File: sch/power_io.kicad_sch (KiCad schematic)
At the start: 5 parts

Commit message: mp1584
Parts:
- added U?: MP1584EN-LF-Z, usb_xwitch:MP1584EN-LF-Z, symbol usb_xwitch:MP1584EN-LF-Z
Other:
- note added: "Comms / PWR from Raspberry Pi as a HAT"
- moved on the sheet: D?, J?, TP?

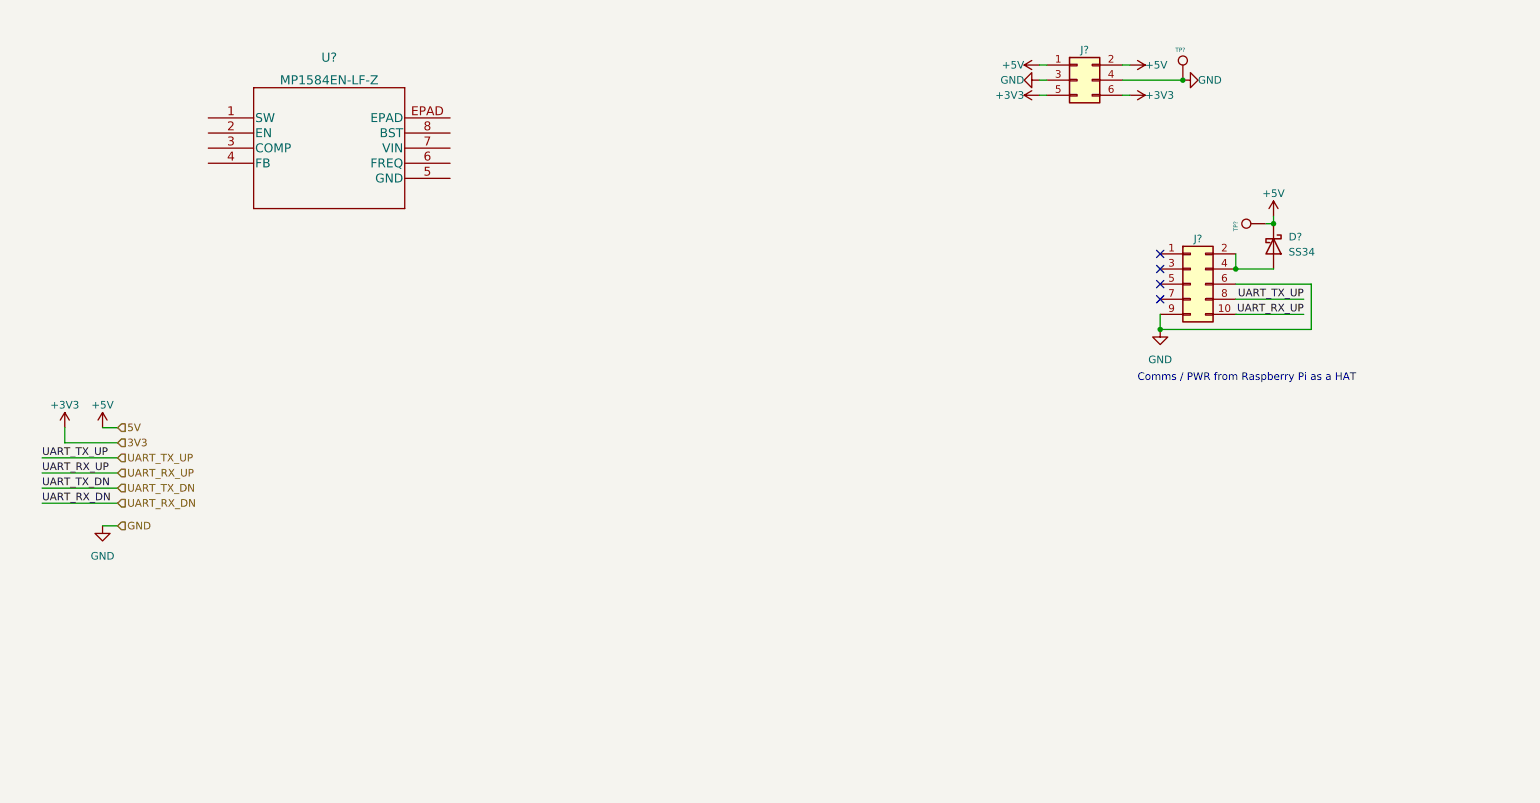
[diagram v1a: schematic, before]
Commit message: updated power circuit
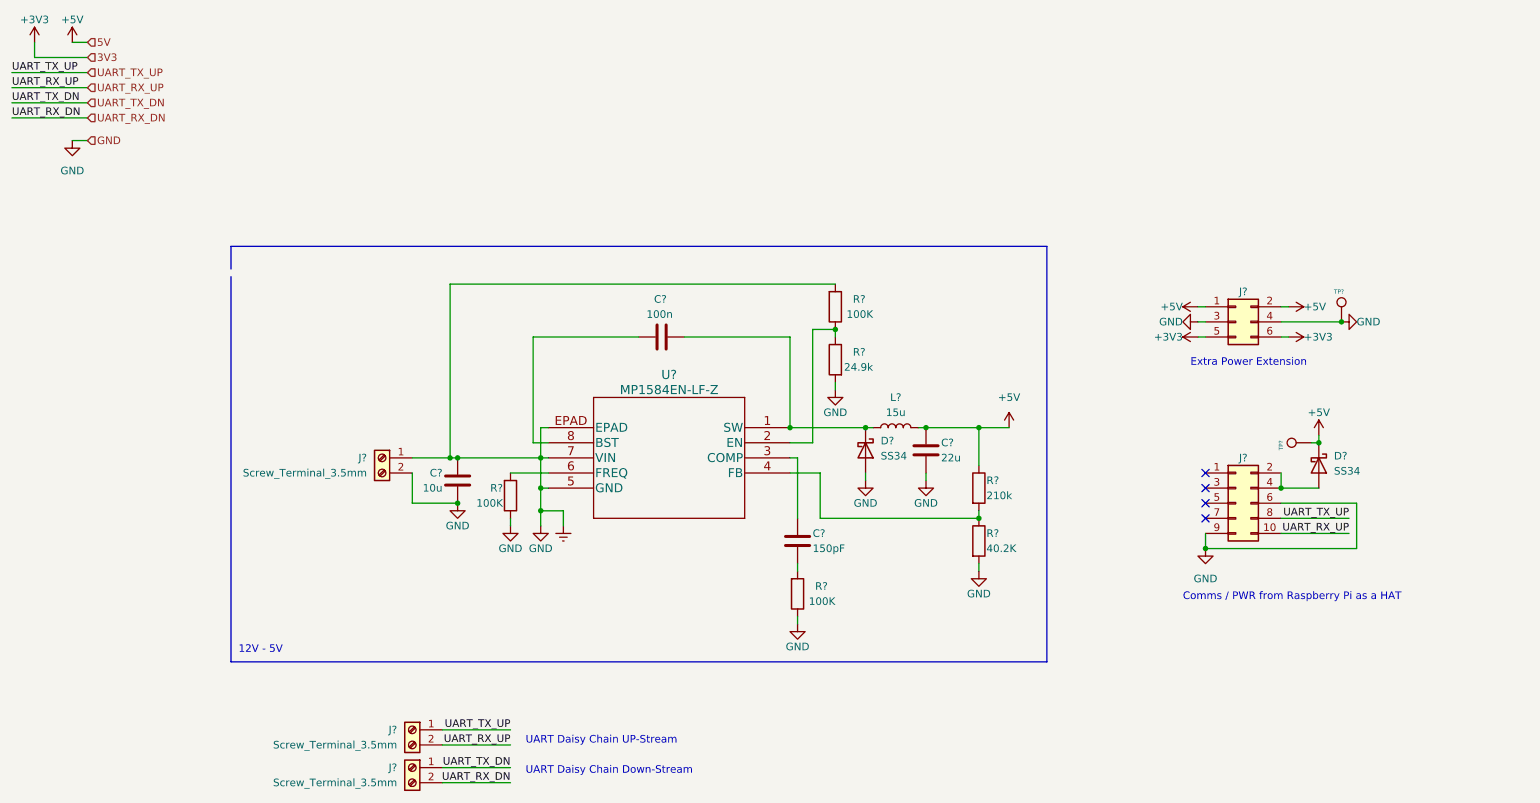
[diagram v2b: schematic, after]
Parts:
- added C?: 22u, Capacitor_SMD:C_1206_3216Metric_Pad1.33x1.80mm_HandSolder, symbol Device:C
- added C?: 100n, Resistor_SMD:R_0402_1005Metric_Pad0.72x0.64mm_HandSolder, symbol Device:C
- added C?: 10u, Capacitor_SMD:C_0805_2012Metric_Pad1.18x1.45mm_HandSolder, symbol Device:C
- added C?: 150pF, Resistor_SMD:R_0402_1005Metric_Pad0.72x0.64mm_HandSolder, symbol Device:C
- added D?: SS34, Diode_SMD:D_SMA, symbol Device:D_Schottky
- added J? (x3): Screw_Terminal_3.5mm, TerminalBlock_4Ucon:TerminalBlock_4Ucon_1x02_P3.50mm_Horizontal, symbol Connector:Screw_Terminal_01x02
- added L?: 15u, Inductor_SMD:L_12x12mm_H6mm, symbol Device:L
- added R? (x3): 100K, Resistor_SMD:R_0402_1005Metric_Pad0.72x0.64mm_HandSolder, symbol Device:R
- added R?: 210k, Resistor_SMD:R_0402_1005Metric_Pad0.72x0.64mm_HandSolder, symbol Device:R
- added R?: 24.9k, Resistor_SMD:R_0603_1608Metric_Pad0.98x0.95mm_HandSolder, symbol Device:R
- added R?: 40.2K, Resistor_SMD:R_0402_1005Metric_Pad0.72x0.64mm_HandSolder, symbol Device:R
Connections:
- net GND is gone; now on net Earth: J?.3 (Pin_3), J?.4 (Pin_4), J?.6 (Pin_6), J?.9 (Pin_9), TP?.1
- net +5V: now also C?.1, L?.2, R?.1
- net UART_RX_DN: now also J?.2 (Pin_2)
- net UART_RX_UP: now also J?.2 (Pin_2)
- net UART_TX_DN: now also J?.1 (Pin_1)
- net UART_TX_UP: now also J?.1 (Pin_1)
- net at U?.1 (SW): now also C?.1, D?.1 (K), L?.1
- net at U?.2 (EN): now also R?.1, R?.1
- net at U?.3 (COMP): now also C?.1
- net at U?.4 (FB): now also R?.1, R?.2
- net Earth: now reaches U?.5 (GND)
- net Earth: now also U?.7 (VIN), U?.EPAD, C?.1, C?.2, C?.2, D?.2 (A), J?.1 (Pin_1), J?.2 (Pin_2), R?.1, R?.1, R?.2, R?.2, R?.2
- net at U?.6 (FREQ): now also R?.2
- net at U?.8 (BST): now also C?.2
- new net: C?.2, R?.2
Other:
- note added: "12V - 5V"
- note added: "Extra Power Extension"
- note added: "UART Daisy Chain Down-Stream"
- note added: "UART Daisy Chain UP-Stream"
- moved on the sheet: D?, J?, TP?, U?

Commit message: annotated components
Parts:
- J11: renamed from J?; LCSC (none) -> C65114
- U8: renamed from U?; LCSC (none) -> C15051
- gave numbers to parts that had none: 19

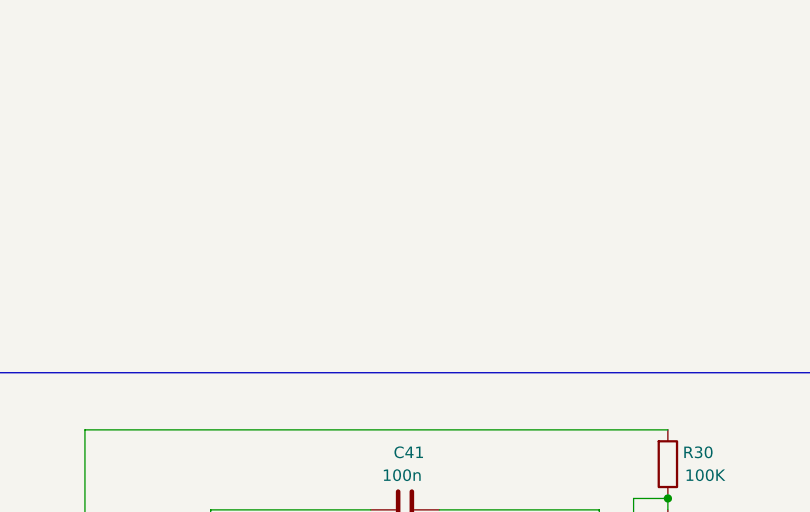
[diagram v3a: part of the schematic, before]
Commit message: drc checks and renaming
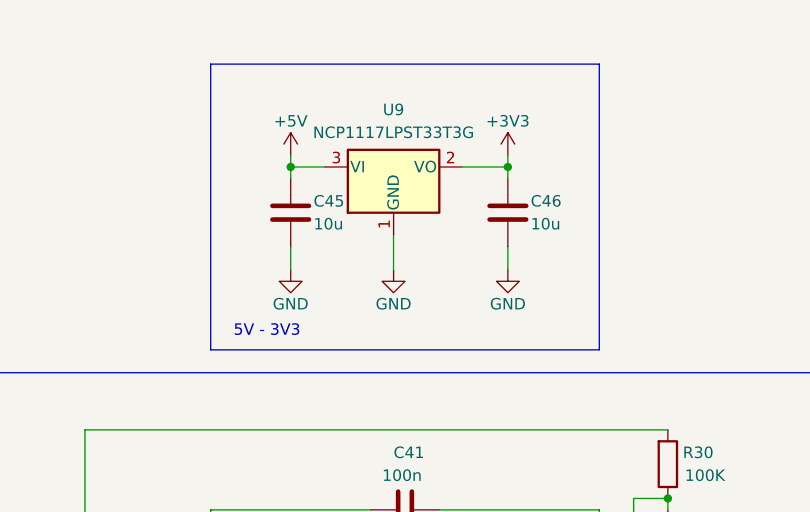
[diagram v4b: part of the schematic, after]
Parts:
- added C45, C46: 10u, Capacitor_SMD:C_0603_1608Metric_Pad1.08x0.95mm_HandSolder, symbol Device:C
- added U9: NCP1117LPST33T3G, Package_TO_SOT_SMD:SOT-223-3_TabPin2, symbol Regulator_Linear:NCP1117-3.3_SOT223
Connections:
- net +3V3: now also C46.1, U9.2 (VO)
- net +5V: now also C45.1, U9.3 (VI)
- net Earth: now also C45.2, C46.2, U9.1 (GND)
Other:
- note added: "5V - 3V3"

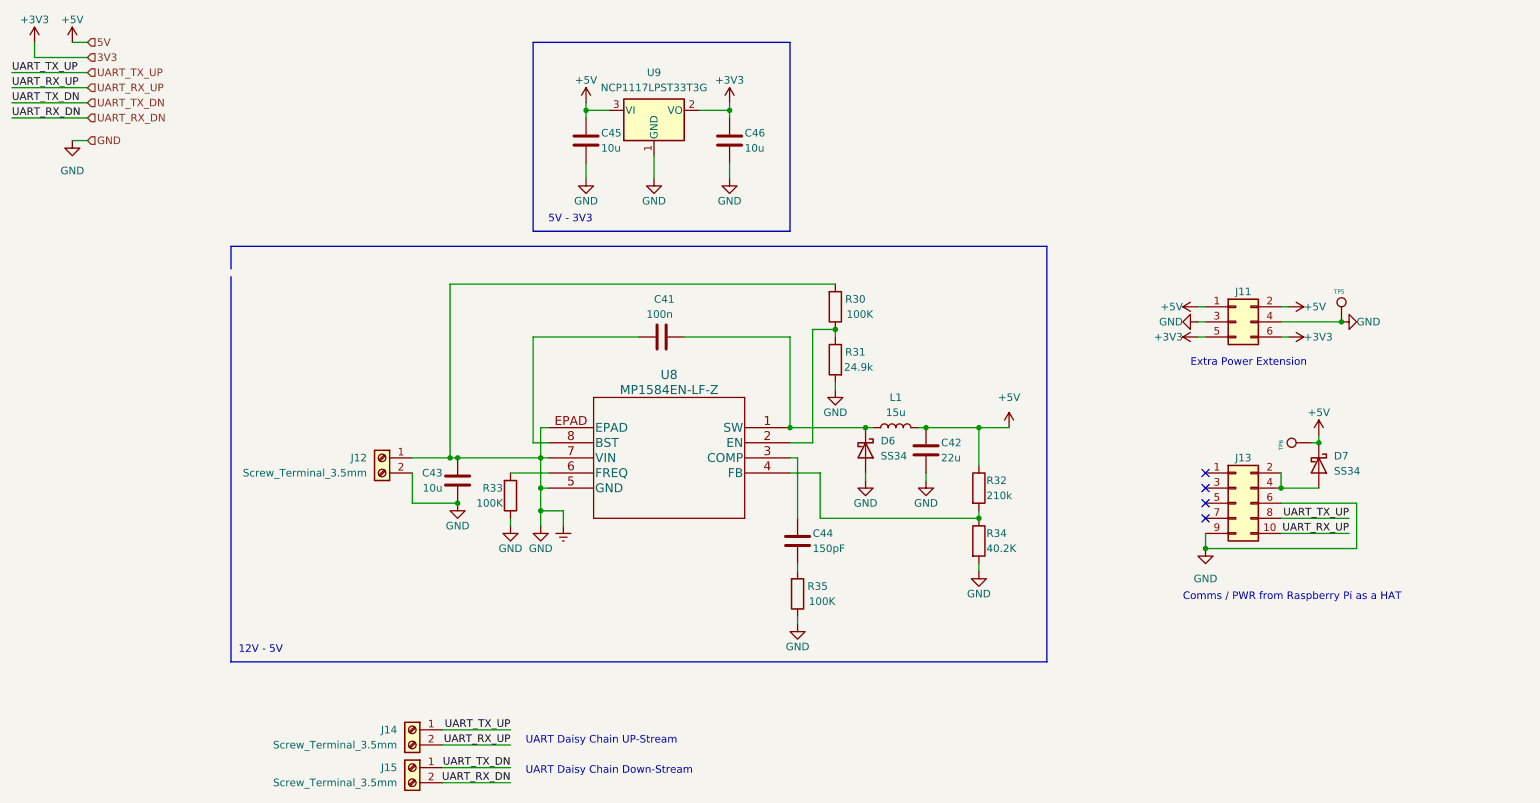
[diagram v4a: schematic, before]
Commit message: updated power on leds, hub 4 LEDs and misc
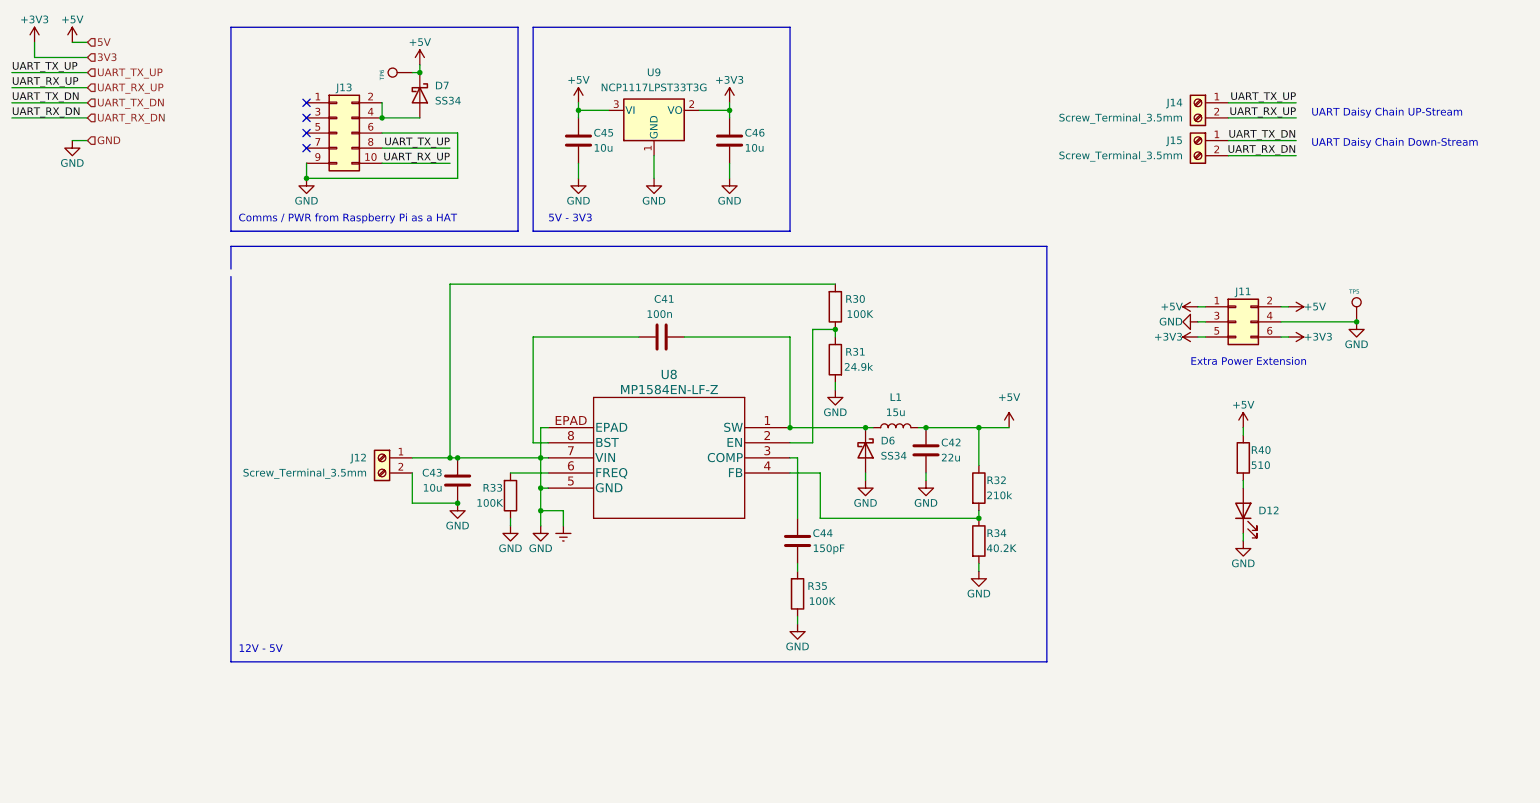
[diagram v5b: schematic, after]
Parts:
- added D12: 19-217/GHC-YR1S2/3T, Diode_SMD:D_0603_1608Metric_Pad1.05x0.95mm_HandSolder, symbol Device:LED
- added R40: 510, Resistor_SMD:R_0402_1005Metric_Pad0.72x0.64mm_HandSolder, symbol Device:R
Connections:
- net +5V: now also R40.1
- net Earth: now also D12.1 (K)
- new net: D12.2 (A), R40.2
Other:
- moved on the sheet: C45, D7, J13, J14, J15, TP5, TP6

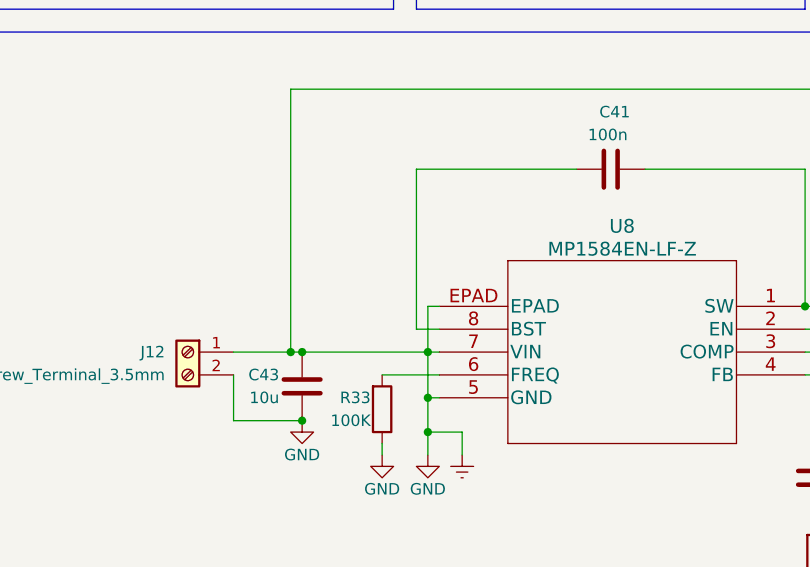
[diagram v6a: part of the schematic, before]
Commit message: fix sch unexpect to gnd; usb to right angle; pcb boarder increased to pi size
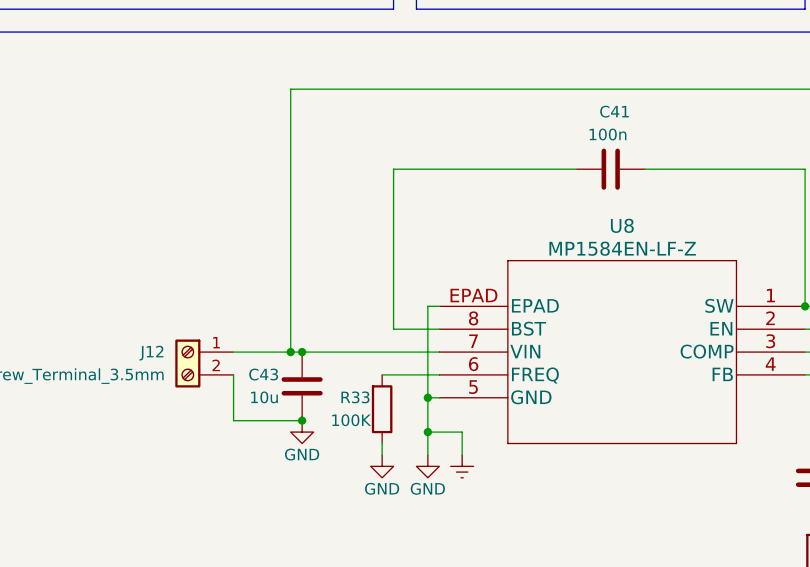
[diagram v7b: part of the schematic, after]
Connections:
- net Earth: no longer C43.1, J12.1 (Pin_1), R30.2, U8.7 (VIN)
- new net: C43.1, J12.1 (Pin_1), R30.2, U8.7 (VIN)
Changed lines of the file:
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@@
   (junction (at 124.46 41.91) (diameter 0) (color 0 0 0 0)
   )
-  (junction (at 118.11 100.33) (diameter 0) (color 0 0 0 0)
+  (junction (at 102.87 100.33) (diameter 0) (color 0 0 0 0)
   )
   (junction (at 191.77 110.49) (diameter 0) (color 0 0 0 0)
@@
   (junction (at 255.27 77.47) (diameter 0) (color 0 0 0 0)
   )
-  (junction (at 102.87 100.33) (diameter 0) (color 0 0 0 0)
-  )
   (junction (at 78.74 53.34) (diameter 0) (color 0 0 0 0)
   )
@@
   (junction (at 91.44 43.18) (diameter 0) (color 0 0 0 0)
   )
+  (junction (at 118.11 105.41) (diameter 0) (color 0 0 0 0)
+  )
   (junction (at 118.11 109.22) (diameter 0) (color 0 0 0 0)
   )
   (junction (at 97.79 35.56) (diameter 0) (color 0 0 0 0)
-  )
-  (junction (at 118.11 105.41) (diameter 0) (color 0 0 0 0)
   )
   (junction (at 104.14 100.33) (diameter 0) (color 0 0 0 0)
@@
     (stroke (width 0) (type default) (color 0 0 0 0))
   )
-  (wire (pts (xy 102.87 100.33) (xy 96.52 100.33))
-    (stroke (width 0) (type default) (color 0 0 0 0))
-  )
   (polyline (pts (xy 203.2 64.77) (xy 66.04 64.77))
     (stroke (width 0) (type default) (color 0 0 0 0))
@@
     (stroke (width 0) (type default) (color 0 0 0 0))
   )
+  (wire (pts (xy 118.11 95.25) (xy 118.11 105.41))
+    (stroke (width 0) (type default) (color 0 0 0 0))
+  )
   (wire (pts (xy 167.64 78.74) (xy 167.64 80.01))
     (stroke (width 0) (type default) (color 0 0 0 0))
@@
     (stroke (width 0) (type default) (color 0 0 0 0))
   )
-  (wire (pts (xy 118.11 100.33) (xy 118.11 105.41))
-    (stroke (width 0) (type default) (color 0 0 0 0))
-  )
   (polyline (pts (xy 66.04 134.62) (xy 203.2 134.62))
     (stroke (width 0) (type default) (color 0 0 0 0))
@@
     (stroke (width 0) (type default) (color 0 0 0 0))
   )
-  (wire (pts (xy 116.84 97.79) (xy 119.38 97.79))
-    (stroke (width 0) (type default) (color 0 0 0 0))
-  )
-  (wire (pts (xy 118.11 100.33) (xy 104.14 100.33))
+  (wire (pts (xy 114.3 97.79) (xy 119.38 97.79))
     (stroke (width 0) (type default) (color 0 0 0 0))
   )
@@
     (stroke (width 0) (type default) (color 0 0 0 0))
   )
-  (wire (pts (xy 118.11 95.25) (xy 118.11 100.33))
-    (stroke (width 0) (type default) (color 0 0 0 0))
-  )
-  (wire (pts (xy 134.62 80.01) (xy 116.84 80.01))
+  (wire (pts (xy 134.62 80.01) (xy 114.3 80.01))
     (stroke (width 0) (type default) (color 0 0 0 0))
   )
@@
     (stroke (width 0) (type default) (color 0 0 0 0))
   )
-  (wire (pts (xy 116.84 80.01) (xy 116.84 97.79))
-    (stroke (width 0) (type default) (color 0 0 0 0))
-  )
-  (wire (pts (xy 118.11 100.33) (xy 119.38 100.33))
+  (wire (pts (xy 114.3 80.01) (xy 114.3 97.79))
+    (stroke (width 0) (type default) (color 0 0 0 0))
+  )
+  (wire (pts (xy 104.14 100.33) (xy 119.38 100.33))
     (stroke (width 0) (type default) (color 0 0 0 0))
   )
@@
     (stroke (width 0) (type default) (color 0 0 0 0))
   )
+  (wire (pts (xy 96.52 100.33) (xy 102.87 100.33))
+    (stroke (width 0) (type default) (color 0 0 0 0))
+  )
